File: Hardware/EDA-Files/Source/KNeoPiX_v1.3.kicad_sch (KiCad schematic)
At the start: 32 parts, among them J1 Conn_KNX, J2 Conn_KNX, J3 Screw Terminal - Non Isolated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, J4 Screw Terminal - Isolated IOs, J5 Open KNX Debug, J6 Conn_01x05, SW1 Prog BTN, U1 Seeeduino XIAO, U2 LM2937IMP-3.3 / 5.0, U3 ADuM1201AR / ADum1250, U4 ADum1250

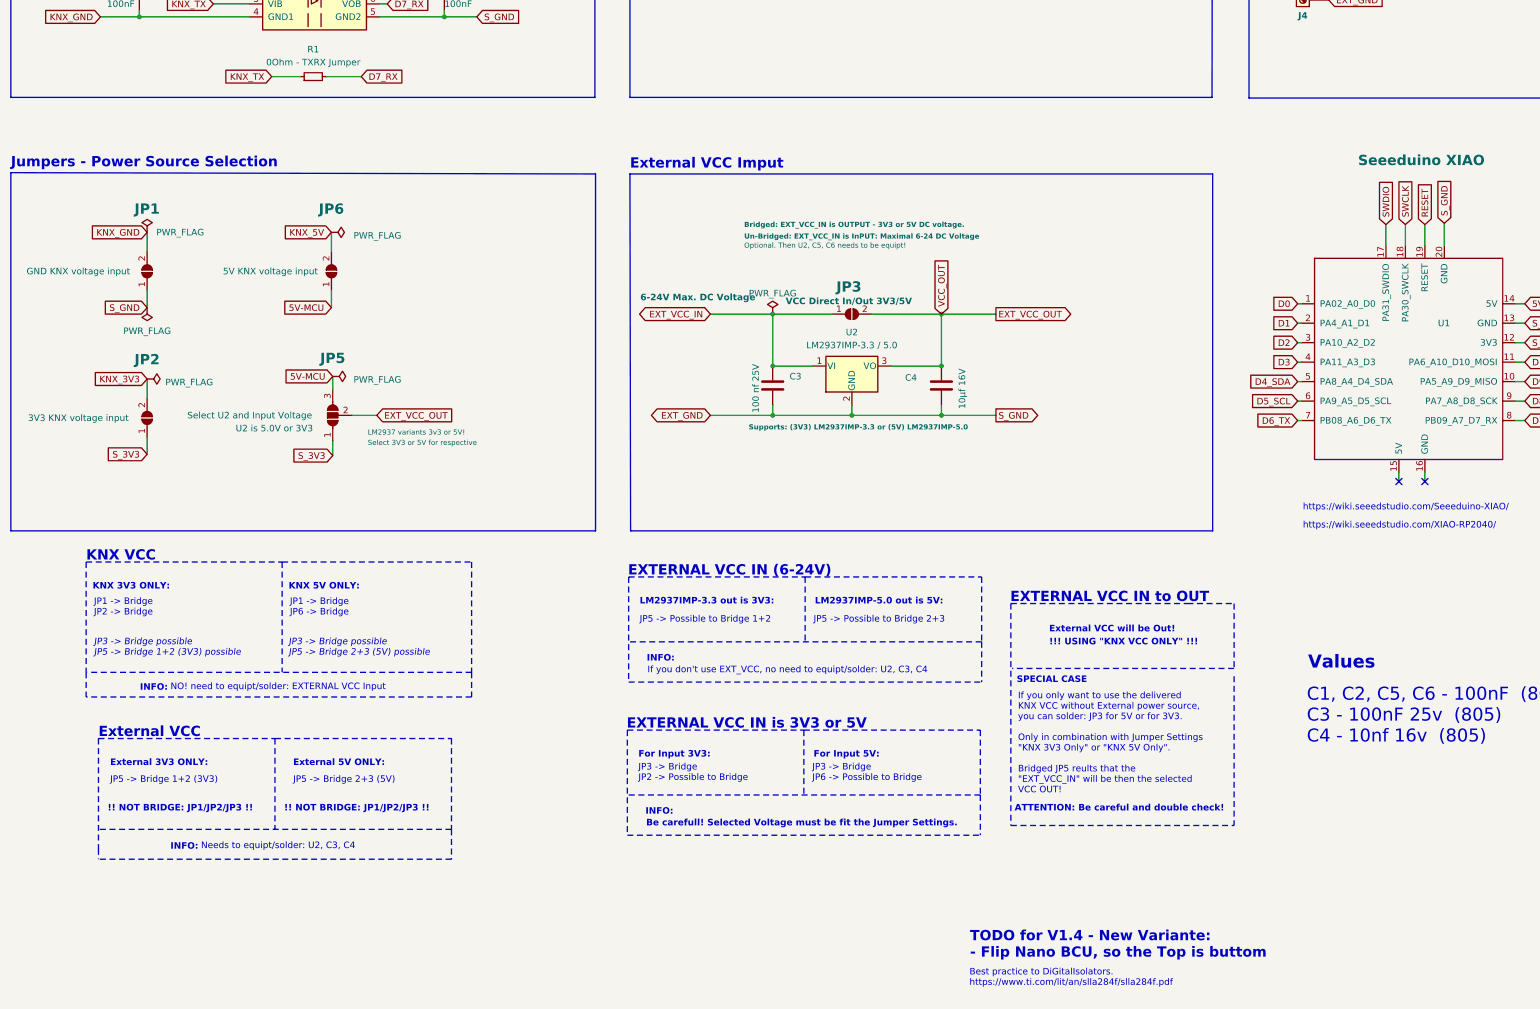
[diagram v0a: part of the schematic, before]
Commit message: Initial draft readme & cleanups
- add Seeed-Studio-XIAO Series SOM datasheet pdf to external documentation
- add pcb renderings
- add Schematic_v1.3 pdf
- cleaned and reorganized Source files
- add. ESP32-C3 step file
- fixed kicad pagelayout
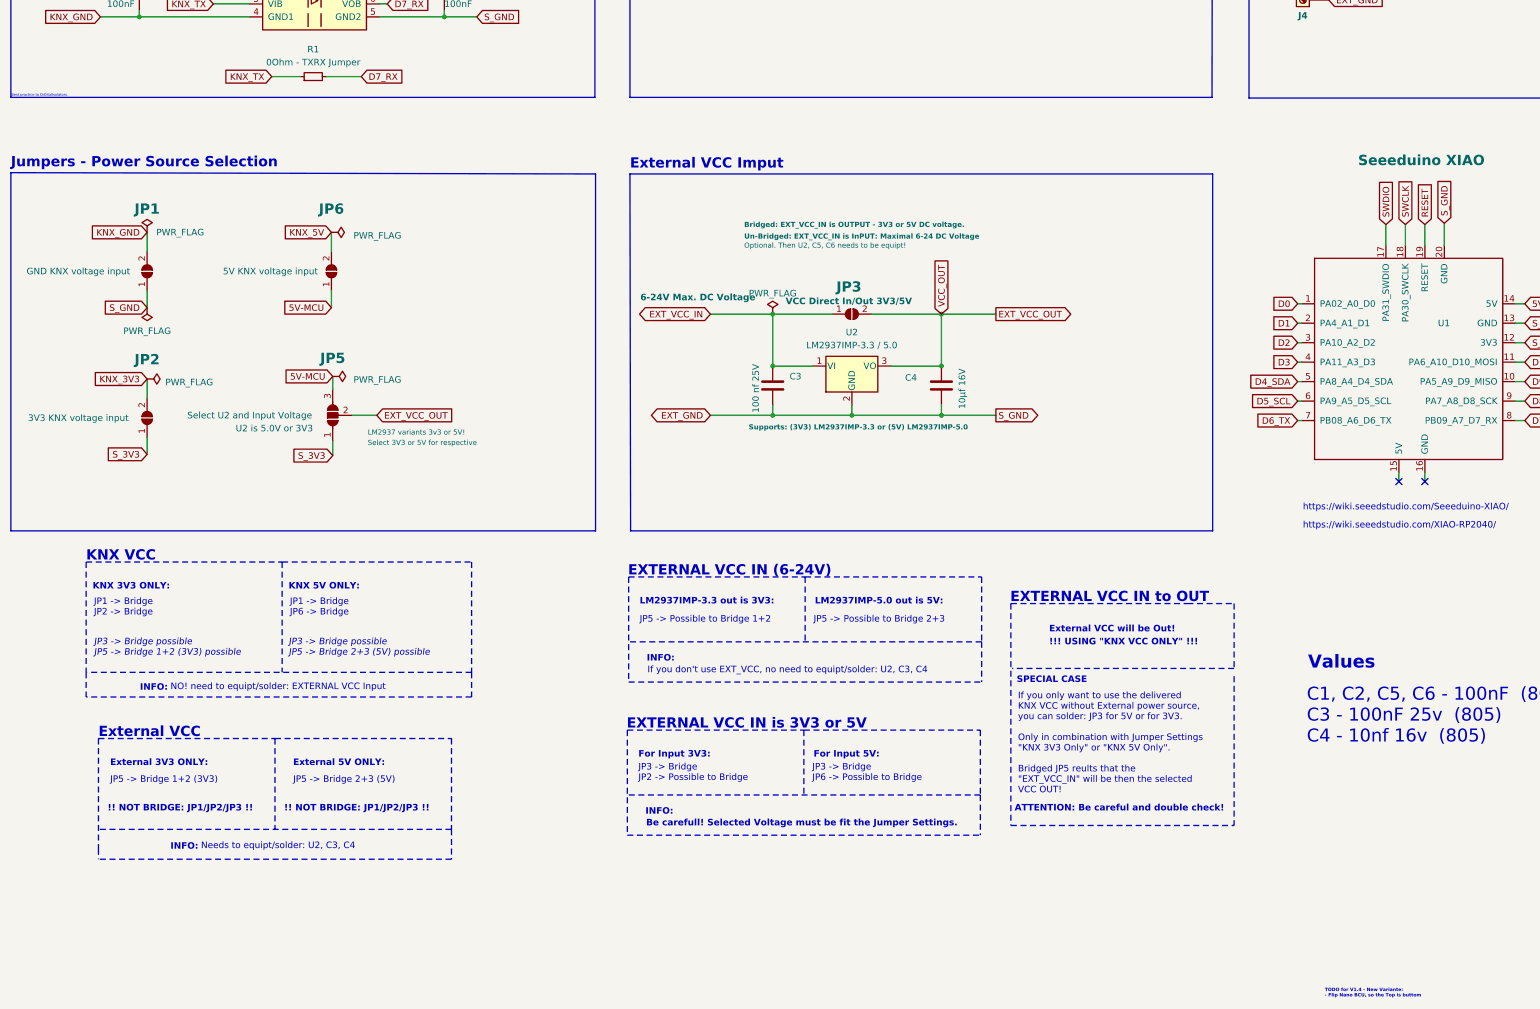
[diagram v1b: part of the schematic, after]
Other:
- note added: "Best practice to DiGitalIsolators."
- note removed: "Best practice to DiGitalIsolators. https://www.ti.com/lit/an/slla284f/slla284f.pdf"
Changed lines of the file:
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@@
   )
   (text "TODO for V1.4 - New Variante: \n- Flip Nano BCU, so the Top is buttom\n"
-    (at 205.74 275.336 0)
-    (effects (font (size 2 2) bold) (justify left bottom))
+    (at 275.1836 282.956 0)
+    (effects (font (size 0.65 0.65) bold) (justify left bottom))
   )
   (text "If you don't use EXT_VCC, no need to equipt/solder: U2, C3, C4"
@@
     (effects (font (size 1.27 1.27)) (justify left bottom))
   )
-  (text "Best practice to DiGitalIsolators.\nhttps://www.ti.com/lit/an/slla284f/slla284f.pdf\n"
-    (at 205.6384 280.7716 0)
-    (effects (font (size 1.27 1.27)) (justify left bottom) (href "https://www.ti.com/lit/an/slla284f/slla284f.pdf"))
-  )
   (text "External 5V ONLY:" (at 73.279 237.744 0)
     (effects (font (size 1.27 1.27) (thickness 0.254) bold) (justify left bottom))
@@
     (effects (font (size 1.27 1.27) (thickness 0.254) bold) (justify right bottom))
   )
+  (text "Best practice to DiGitalIsolators.\n" (at 18.1356 106.68 0)
+    (effects (font (size 0.5 0.5)) (justify left bottom) (href "https://www.ti.com/lit/an/slla284f/slla284f.pdf"))
+  )
   (text "https://wiki.seeedstudio.com/Seeeduino-XIAO/" (at 270.891 187.706 0)

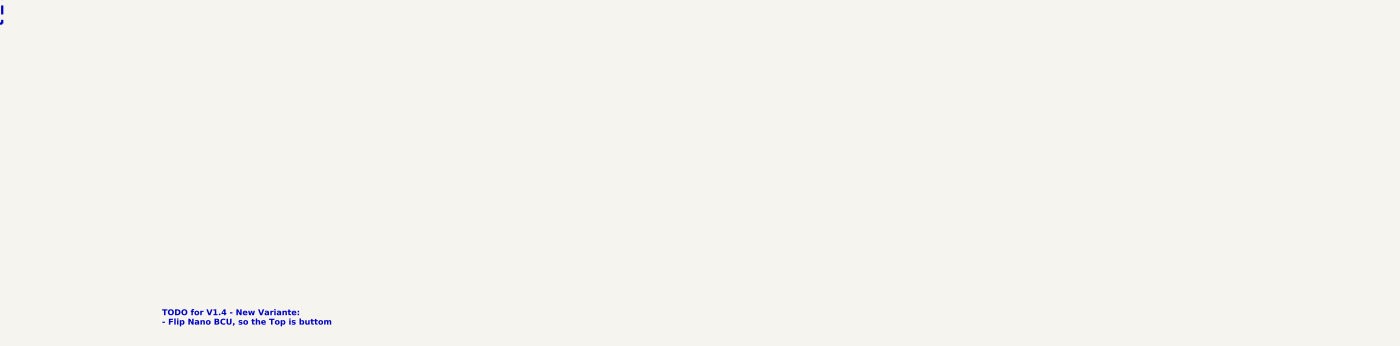
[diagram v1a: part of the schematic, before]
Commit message: Update - KiCad 8.0x
- Fixed Spelling in sch!
- Ignore Thumbs.db
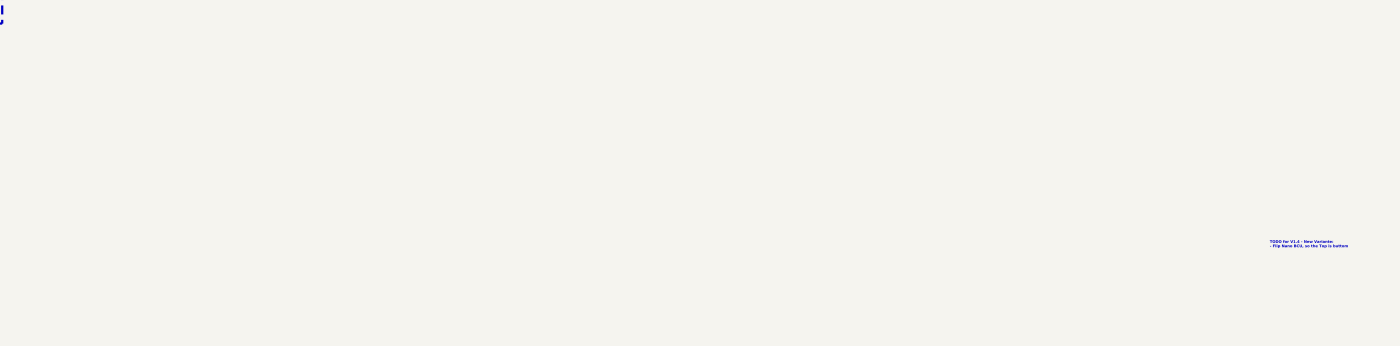
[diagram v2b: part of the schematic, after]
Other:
- title: KNEoPix -> KNeoPix

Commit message: V1.4 - First Prototype Pre Production - In Review
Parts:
- removed C1, C6: 100nF, KNeoPix:C_0805_2012Metric, symbol KNeoPix.symbols:C
- removed C3: 100 nf 25V, KNeoPix:C_0805_2012Metric, symbol KNeoPix.symbols:C
- removed C4: 10µf 16V, KNeoPix:C_0805_2012Metric, symbol KNeoPix.symbols:C
- removed C7: 100nF 16V - (X5R 0805), KNeoPix:C_0805_2012Metric, symbol KNeoPix.symbols:C
- removed D3: SMAJ40CA-13-F, KNeoPix:D_SMA, symbol KNeoPix.symbols:SMAJ40CA-13-F
- removed JP2: 3V3 KNX voltage input, KNeoPix:SolderJumper-2_P1.3mm_Open_Pad1.0x1.5mm, symbol KNeoPix.symbols:SolderJumper_2_Open
- removed JP6: 5V KNX voltage input, KNeoPix:SolderJumper-2_P1.3mm_Open_Pad1.0x1.5mm, symbol KNeoPix.symbols:SolderJumper_2_Open
- removed R3: 0Ohm - D4 Jumper, KNeoPix:R_0402_1005Metric_Pad0.72x0.64mm_HandSolder, symbol KNeoPix.symbols:R_Small
- removed R4: 0Ohm - D5 Jumper, KNeoPix:R_0402_1005Metric_Pad0.72x0.64mm_HandSolder, symbol KNeoPix.symbols:R_Small
- removed SW1: Prog BTN, KNeoPix:SW_Push_1P1T_NO_CK_KMR2, symbol KNeoPix.symbols:SW_Push
- removed U1: Seeeduino XIAO, KNeoPix:Seeeduino XIAO-MOUDLE14P-2.54-21X17.8MM-no-15-16-17-18-19-20-pad, symbol KNeoPix.symbols:SeeeduinoXIAO
- removed U2: LM2937IMP-3.3 / 5.0, KNeoPix:SOT-223-3_TabPin2, symbol KNeoPix.symbols:LM2937xMP
- removed U4: ADum1250, KNeoPix:SOIC-8_3.9x4.9mm_P1.27mm, symbol KNeoPix.symbols:ADuM1201AR
- added C10, C9: 22uf/16V, Capacitor_SMD:C_0805_2012Metric, symbol lcsc:CL10A105KB8NNNC
- added C20, C22, C25, C29: 22uf, Capacitor_SMD:C_0402_1005Metric, symbol KNeoPix.symbols:C
- added C21, C23, C24, C26, C27, C28: 220uf, Capacitor_SMD:C_1206_3216Metric, symbol KNeoPix.symbols:C
- added C3, C4: 100nF/16v, Capacitor_SMD:C_01005_0402Metric, symbol lcsc:CC0805KRX7R9BB104
- added C5: 100nF/16v, Capacitor_SMD:C_01005_0402Metric, symbol KNeoPix.symbols:C
- added C6, C7: 10uf/50V, Capacitor_SMD:C_0805_2012Metric, symbol lcsc:CL21A106KAYNNNE
- added C8: 100nF/50v, Capacitor_SMD:C_0805_2012Metric, symbol lcsc:CC0805KRX7R9BB104
- added D1, D2: DIODE SCHOTTKY 40V SOD-323HE, lcsc:SOD-323_L1.7-W1.3-LS2.6-RD-1, symbol lcsc:PD3S230L-TP
- added JP5: SolderJumper_3_Bridged12, Jumper:SolderJumper-3_P1.3mm_Bridged2Bar12_Pad1.0x1.5mm, symbol Jumper:SolderJumper_3_Bridged12
- added L1: CR5040-4R7M, lcsc:IND-SMD_L5.0-W5.0, symbol lcsc:CR5040-4R7M
- added R20: 10K, Resistor_SMD:R_0402_1005Metric, symbol Device:R_Small
- added SW1: PROG BUTTON, lcsc:KEY-SMD_4P-L4.2-W3.2-P2.20-LS4.6, symbol lcsc:SKRPACE010
- added U1: Seeeduino XIAO, Xiao-ESP32S3-Extendet-Pads:Seeeduino XIAO-MOUDLE14P-2.54-21X17.8MM-no-15-16-17-18-19-20-pad, symbol xiao:SeeeduinoXIAO
- added U2: TXS0108EPWR, lcsc:TSSOP-20_L6.5-W4.4-P0.65-LS6.4-BL, symbol lcsc:TXS0108EPWR
- added U20: AP2112K-3.3, Package_TO_SOT_SMD:SOT-23-5, symbol Regulator_Linear:AP2112K-3.3
- added U21: LM66200DRLR, Package_TO_SOT_SMD:SOT-583-8, symbol lcsc:LM66200DRLR
- added U5: AP63205WU-7, lcsc:TSOT-26_L2.9-W1.6-P0.95-LS2.8-BL, symbol lcsc:AP63203WU-7
- C1: renamed from C2; value 100nF -> 100nF/16v; footprint KNeoPix:C_0805_2012Metric -> Capacitor_SMD:C_01005_0402Metric; LCSC Part (none) -> C60474
- C2: renamed from C5; value 100nF -> 100nF/16v; footprint KNeoPix:C_0805_2012Metric -> Capacitor_SMD:C_01005_0402Metric; LCSC Part (none) -> C60474
- GN1, J1, J2, JP4: now left out of the parts list
- J3: value Screw Terminal - Non Isolated IOs -> Screw Terminal - Isolated IOs
- J5: value Open KNX Debug -> ~; lcsc (none) -> C160391
- J6: now not fitted; now left out of the parts list
- JP1: value GND KNX voltage input -> KNX GND Input; now left out of the parts list
- JP2: renamed from JP5; value Select U2 and Input Voltage -> EXT Input Voltage; now left out of the parts list
- JP3: value VCC Direct In/Out 3V3/5V -> KNX Voltage Input; footprint KNeoPix:SolderJumper-2_P1.3mm_Open_Pad1.0x1.5mm -> Jumper:SolderJumper-2_P1.3mm_Open_Pad1.0x1.5mm; now not fitted; now left out of the parts list
- R1, R2: now not fitted
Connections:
- net NEO_DATA0_OUT is gone; now on net EXT_GND: J4.2 (Pin_2)
- net 5V-MCU: now also J3.3 (Pin_3), JP2.2 (C), JP5.1 (A), U1.14 (5V); no longer JP2.3 (B)
- net D0: now also C5.1, SW1.1, SW1.2, U1.1 (PA02_A0_D0)
- net D1: now also U1.2 (PA4_A1_D1), U2.1 (A1); no longer J3.4 (Pin_4)
- net D10: now also U1.11 (PA6_A10_D10_MOSI), U2.9 (A8); no longer J3.9 (Pin_9)
- net D2: now also U1.3 (PA10_A2_D2), U2.3 (A2); no longer J3.5 (Pin_5)
- net D3: now also U1.4 (PA11_A3_D3), U2.4 (A3); no longer J3.6 (Pin_6)
- net D6_TX: now also U1.7 (PB08_A6_D6_TX)
- net D7_RX: now also U1.8 (PB09_A7_D7_RX)
- net D8: now also U1.9 (PA7_A8_D8_SCK), U2.7 (A6); no longer J3.7 (Pin_7)
- net D9: now also U1.10 (PA5_A9_D9_MISO), U2.8 (A7); no longer J3.8 (Pin_8)
- net EXT_GND: now also C10.2, C3.1, C4.1, C6.2, C7.2, C9.1, U1.13 (GND), U1.20 (GND), U2.11 (GND), U5.4 (GND); no longer J4.1 (Pin_1), J5.1 (Pin_1), J6.1 (Pin_1)
- net EXT_VCC_IN: now also J4.1 (Pin_1), C6.1, C7.1, U5.2 (EN), U5.3 (VIN); no longer J4.4 (Pin_4), JP3.1 (A)
- net KNX_3V3: now also JP3.1 (A), C23.1, C24.1, C25.2, U21.6 (VIN2)
- net KNX_5V: now also C20.2, C21.1, D1.2 (A), U20.1 (VIN), U20.3 (EN); no longer J3.3 (Pin_3)
- net KNX_GND: now also C20.1, C21.2, C22.2, C23.2, C24.2, C25.1, C26.1, C27.2, C28.2, C29.1, C5.2, R20.2, SW1.3, SW1.4, U20.2 (GND), U21.1 (GND), U21.5 (GND)
- net EXT_VCC_OUT renamed 3v3-MCU
- net 3v3-MCU: now also C2.1, J3.2 (Pin_2), U3.8 (VDD2), C26.2, C27.1, C28.1, C29.2, C3.2, JP5.3 (B), U1.12 (3V3), U2.10 (OE), U2.2 (VCCA), U21.2 (VOUT), U21.7 (VOUT); no longer JP2.2 (C)
- net NEO_DATA1_OUT renamed DL4
- net DL4: now also U2.16 (B4)
- net RESET renamed RESET/EN
- net RESET/EN: now also U1.19 (RST/EN)
- net SWCLK renamed CLK/MTDO
- net CLK/MTDO: now also U1.18 (CLK/MTDO)
- net SWDIO renamed DIO/MTDI
- net DIO/MTDI: now also U1.17 (DIO/MTDI)
- removed net S_3V3: C2.1, J3.2 (Pin_2), J5.2 (Pin_2), J6.2 (Pin_2), JP2.1 (A), U3.8 (VDD2)
- new net: C22.1, U20.5 (VOUT), U21.3 (VIN1)
- new net: R20.1, U21.4 (~{ON})
- new net: C8.2, L1.1, U5.5 (SW)
- new net: D1.1 (K), JP2.3 (B)
- new net: D2.1 (K), JP2.1 (A)
- new net: C8.1, U5.6 (BST)
- new net 3v3/MTCK: J5.2 (Pin_2), J6.2 (Pin_2), U1.21 (3V3/MTCK)
- new net BOOT/MTMS: J5.1 (Pin_1), J6.1 (Pin_1), U1.22 (BOOT/MTMS)
- new net D4: U1.5 (PA8_A4_D4_SDA), U2.5 (A4)
- new net D5: U1.6 (PA9_A5_D5_SCL), U2.6 (A5)
- new net DL1: J3.4 (Pin_4), U2.20 (B1)
- new net DL10: J3.9 (Pin_9), U2.12 (B8)
- new net DL2: J3.5 (Pin_5), U2.18 (B2)
- new net DL3: J3.6 (Pin_6), U2.17 (B3)
- new net DL5: J4.4 (Pin_4), U2.15 (B5)
- new net DL8: J3.7 (Pin_7), U2.14 (B6)
- new net DL9: J3.8 (Pin_8), U2.13 (B7)
- new net EXT_5V: C10.1, C9.2, D2.2 (A), L1.2, U5.1 (FB)
- new net VCC_LS: C4.2, JP5.2 (C), U2.19 (VCCB)
- no-connect marks 2 -> 3
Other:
- note added: "Default Configuration (External Power Supply): - JP1: OPEN - JP2: Position 1-2 (EXT_5V to 5V-MCU) - Power Input: 5-32V DC via EXT_VCC_IN - Isolation: Active (galvanically isolated via ADUM1201) - Ground: GNDA (KNX) and GNDB (External) separated Alternative Configuration (KNX Bus Power): - JP1: CLOSED (pins 1-2 bridged) - JP2: Position 2-3 (KNX_5V to 5V-MCU) - Power Source: KNX bus via NCN5130 - I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"
- note added: "Internal VCC Input"
- note added: "KNX_5V: If used for 5V-MCU - No isolation on isolator (U3). U3 will be deacktivated and will act as a level shifter 3v3<->3v3!"
- note added: "KNX_GND only in combination: - with KNX_5V for 5V-MCU"
- note added: "Levelshifter"
- note added: "NCN5130 - VDD1 Input"
- note added: "NCN5130 - VDD2 Input"
- note added: "Output to MCU 3V3"
- note added: "POWER SOURCE SELECTION - JUMPER CONFIGURATION"
- note added: "https://wiki.seeedstudio.com/XIAO-ESP32S3/"
- note removed: "!!! USING "KNX VCC ONLY" !!!"
- note removed: "ATTENTION: Be careful and double check!"
- note removed: "C1, C2, C5, C6 - 100nF (805) C3 - 100nF 25v (805) C4 - 10nf 16v (805)"
- note removed: "Digital Isolator GPIO4 & GPIO5"
- note removed: "EXTERNAL VCC IN to OUT"
- note removed: "External VCC will be Out!"
- note removed: "If you only want to use the delivered KNX VCC without External power source, you can solder: JP3 for 5V or for 3V3. Only in combination with Jumper Settings "KNX 3V3 Only" or "KNX 5V Only". Bridged JP5 reults that the "EXT_VCC_IN" will be then the selected VCC OUT!"
- note removed: "KNX RX LED - Blue (Build in LED) Data Pin: D12 SW: Indicate KNX RX-States"
- note removed: "KNX RX LED - Blue (Build in LED) Data Pin: D25 SW: Indicate KNX RX-States"
- note removed: "KNX TX LED - Blue (Build in LED) Data Pin: D11 SW: Indicate KNX TX-States"
- note removed: "KNX TX LED - Green (Build in LED) Data Pin: D16 SW: Indicate KNX TX-States"
- note removed: "Prog LED - RGB LED (Build in NEOPIXEL LED) Data Pin: D12 SW: Indicate PRG-State"
- note removed: "Prog LED - Yellow (Build in LED) Data Pin: D13 SW: Indicate PRG-State"
- note removed: "SPECIAL CASE"
- note removed: "Seeeduino XIAO (ATSAMD21G18A-MU)"
- note removed: "Seeeduino XIAO RP2040"
- note removed: "Values"
- moved on the sheet: C1, C2, GN1, H1, H2, J1, J2, J3, J4, J5, JP1, JP2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

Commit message: Fixed - Prog button GND bug (after Review)
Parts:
- GN1: lcsc (none) -> C2886701
- U3: value ADuM1201AR / ADum1250 -> ADUM1250ARZ-RL7 - (ADuM1201AR / ADum1250AR) AR suffix required; LCSC (none) -> C13839
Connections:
- net EXT_GND: now also C5.2, SW1.3, SW1.4
- net KNX_GND: no longer C5.2, SW1.3, SW1.4
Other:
- note added: "Link: NanoBCU Schematic"
- note added: "Pin SAVE This pin is an open drain output with internal pull-up resistor to VIF. In case of break-down of the bus voltage for more than typ. 1.5 ms (save condition) this pin delivers an active LOW signal to external host electronic. IMPORTANT NOTES: Only use with (KNX Bus Power), else no isolation."
- note removed: "!! NOT BRIDGE: JP1/JP2/JP3 !!"
- note removed: "Be carefull! Selected Voltage must be fit the Jumper Settings."
- note removed: "Best practice to DiGitalIsolators."
- note removed: "EXTERNAL VCC IN (6-24V)"
- note removed: "EXTERNAL VCC IN is 3V3 or 5V"
- note removed: "External 3V3 ONLY:"
- note removed: "External 5V ONLY:"
- note removed: "External VCC"
- note removed: "For Input 3V3:"
- note removed: "For Input 5V:"
- note removed: "INFO:"
- note removed: "If you don't use EXT_VCC, no need to equipt/solder: U2, C3, C4"
- note removed: "JP1 -> Bridge JP2 -> Bridge"
- note removed: "JP1 -> Bridge JP6 -> Bridge"
- note removed: "JP3 -> Bridge JP2 -> Possible to Bridge"
- note removed: "JP3 -> Bridge JP6 -> Possible to Bridge"
- note removed: "JP3 -> Bridge possible JP5 -> Bridge 1+2 (3V3) possible"
- note removed: "JP3 -> Bridge possible JP5 -> Bridge 2+3 (5V) possible"
- note removed: "JP5 -> Bridge 1+2 (3V3)"
- note removed: "JP5 -> Bridge 2+3 (5V)"
- note removed: "JP5 -> Possible to Bridge 1+2"
- note removed: "JP5 -> Possible to Bridge 2+3"
- note removed: "KNX 3V3 ONLY:"
- note removed: "KNX 5V ONLY:"
- note removed: "KNX VCC"
- note removed: "LM2937IMP-3.3 out is 3V3:"
- note removed: "LM2937IMP-5.0 out is 5V:"
- note removed: "NO! need to equipt/solder: EXTERNAL VCC Input"
- note removed: "Needs to equipt/solder: U2, C3, C4"
- note removed: "Pin SAVE This pin is an open drain output with internal pull-up resistor to VIF. In case of break-down of the bus voltage for more than typ. 1.5 ms (save condition) this pin delivers an active LOW signal to external host electronic."
- moved on the sheet: C10, C20, C21, C22, C23, C24, C25, C26, C27, C28, C29, C3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

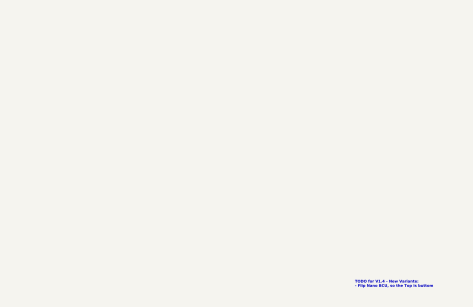
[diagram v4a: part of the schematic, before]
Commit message: AP63205WU-7 (U5) repositioned for better thermal management
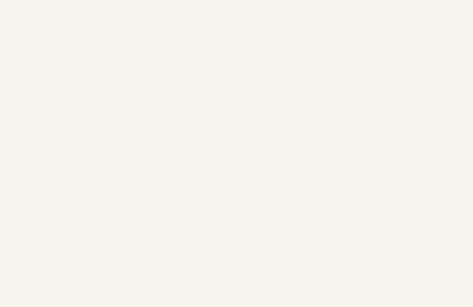
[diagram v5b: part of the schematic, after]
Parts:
- H1, H2: lcsc (none) -> C20252226
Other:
- note removed: "TODO for V1.4 - New Variante: - Flip Nano BCU, so the Top is buttom"
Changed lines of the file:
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@@
 		(title "KNeoPix")
 		(date "2023-02-12")
-		(rev "1.3")
+		(rev "1.4")
 		(company "OpenKNX")
 		(comment 2 "URL: https://github.com/OpenKNX")
@@
 		)
 	)
-	(text "TODO for V1.4 - New Variante: \n- Flip Nano BCU, so the Top is buttom\n"
-		(exclude_from_sim no)
-		(at 398.272 274.32 0)
-		(effects
-			(font
-				(size 0.3 0.3)
-				(bold yes)
-			)
-			(justify left bottom)
-		)
-	)
 	(text "NCN5130 - VDD1 Input"
 		(exclude_from_sim no)
@@
 			)
 		)
+		(property "lcsc" "C20252226"
+			(at 87.63 50.8 0)
+			(effects
+				(font
+					(size 1.27 1.27)
+				)
+				(hide yes)
+			)
+		)
 		(pin "1"
 		)
@@
 				(hide yes)
 			)
+		)
+		(property "lcsc" "C20252226"
+			(at 87.63 36.83 0)
+			(effects
+				(font
+					(size 1.27 1.27)
+				)
+				(hide yes)
+			)
